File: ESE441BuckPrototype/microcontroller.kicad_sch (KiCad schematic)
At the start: 9 parts

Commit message: Add component names, values, PWM jumper
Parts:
- J?: footprint (none) -> Connector_PinHeader_2.54mm:PinHeader_2x04_P2.54mm_Vertical
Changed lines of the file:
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@@
     (property "Reference" "J?" (id 0) (at 228.6 82.55 0))
     (property "Value" "ICSP" (id 1) (at 228.6 85.09 0))
-    (property "Footprint" "" (id 2) (at 227.33 91.44 0)
+    (property "Footprint" "Connector_PinHeader_2.54mm:PinHeader_2x04_P2.54mm_Vertical" (id 2) (at 227.33 91.44 0)
       (effects (font (size 1.27 1.27)) hide)
     )

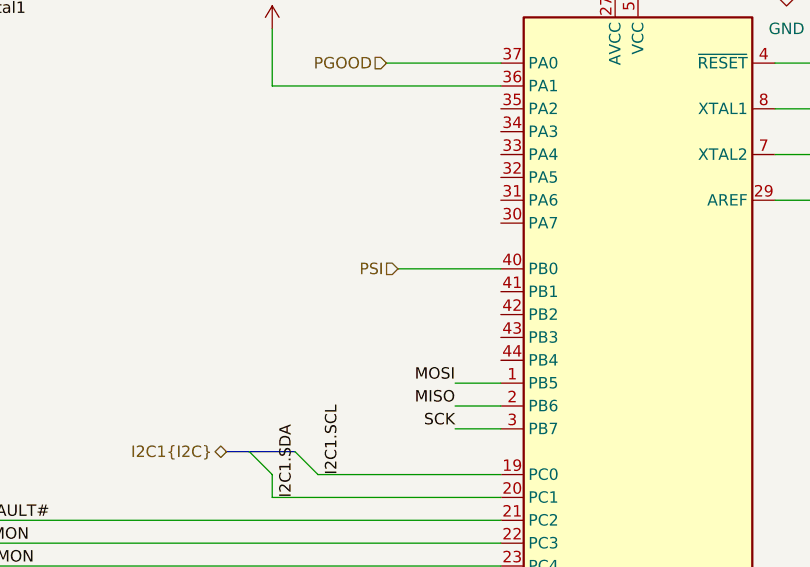
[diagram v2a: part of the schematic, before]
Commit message: Add ALERT# monitoring and fix input/output sheet pins
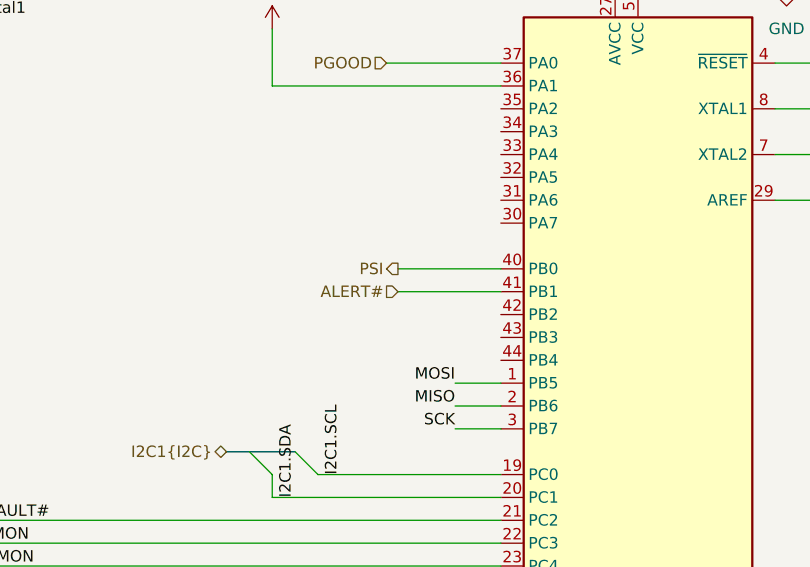
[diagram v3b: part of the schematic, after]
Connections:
- net ALERT#: now reaches U?.41 (PB1)
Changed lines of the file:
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@@
+    (stroke (width 0) (type default) (color 0 0 0 0))
+  )
+  (wire (pts (xy 123.19 95.25) (xy 134.62 95.25))
     (stroke (width 0) (type default) (color 0 0 0 0))
   )
@@
     (effects (font (size 1.27 1.27)) (justify right))
   )
+  (hierarchical_label "ALERT#" (shape input) (at 123.19 95.25 180)
+    (effects (font (size 1.27 1.27)) (justify right))
+  )
   (hierarchical_label "PMon3{PMon}" (shape input) (at 50.8 118.11 180)
     (effects (font (size 1.27 1.27)) (justify right))
   )
-  (hierarchical_label "PSI" (shape input) (at 123.19 92.71 180)
-    (effects (font (size 1.27 1.27)) (justify right))
-  )
+  (hierarchical_label "PSI" (shape output) (at 123.19 92.71 180)
+    (effects (font (size 1.27 1.27)) (justify right))
+  )

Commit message: Add optional LDO and annotations
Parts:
- added C39: 1u-DNP, symbol Device:C_Small
- added C40: 0.1u, symbol Device:C_Small
- added J2, J3: Header, symbol Connector_Generic:Conn_01x02
- added JP2, JP3: Jumper_Open, symbol Jumper:SolderJumper_2_Open
- added JP4: Jumper_Bridged, symbol Jumper:SolderJumper_2_Bridged
- added U5: HT7550-1, Package_TO_SOT_SMD:SOT-23-3, symbol CustomPartsLibrary:HT7550-1
- gave numbers to parts that had none: 9
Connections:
- net +5V: now also J3.1 (Pin_1), JP4.1 (A); no longer C41.1, C42.1, R39.1, U6.17 (VCC), U6.27 (AVCC), U6.38 (VCC), U6.5 (VCC)
- net GND: now also C39.2, C40.2, U5.1 (GND)
- new net: C39.1, JP2.1 (A), U5.2 (VIN)
- new net: C40.1, C41.1, C42.1, J2.2 (Pin_2), J3.2 (Pin_2), JP3.1 (A), JP4.2 (B), R39.1, U6.17 (VCC), U6.27 (AVCC), U6.38 (VCC), U6.5 (VCC)
- new net: J2.1 (Pin_1), JP3.2 (B), U5.3 (VOUT)
- new net VIN: JP2.2 (B)

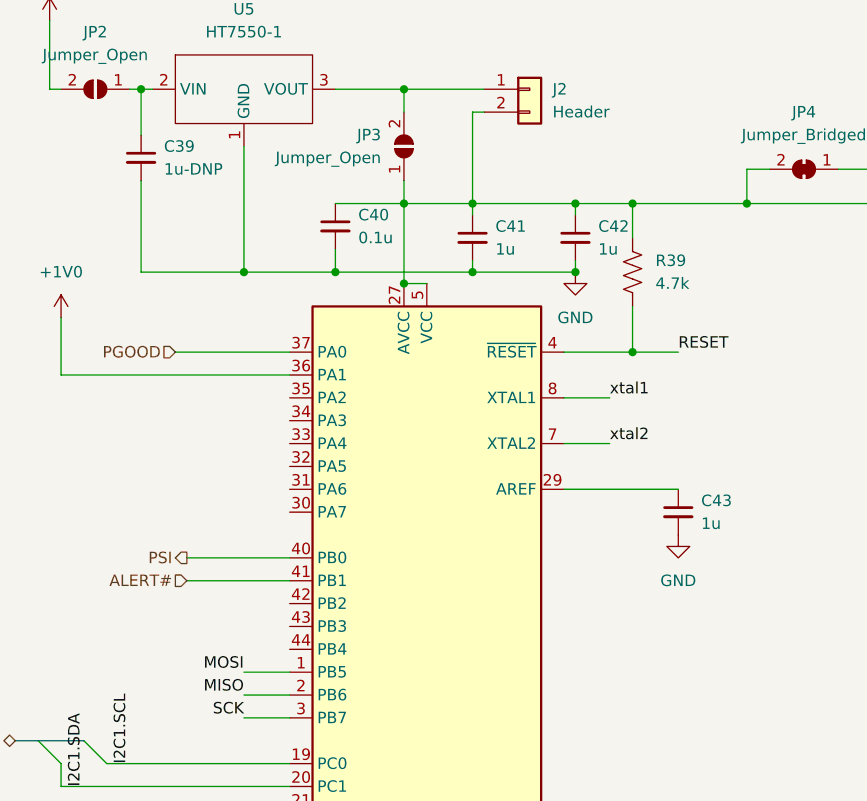
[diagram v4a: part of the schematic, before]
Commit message: Connect enable to MCU; Testpoints
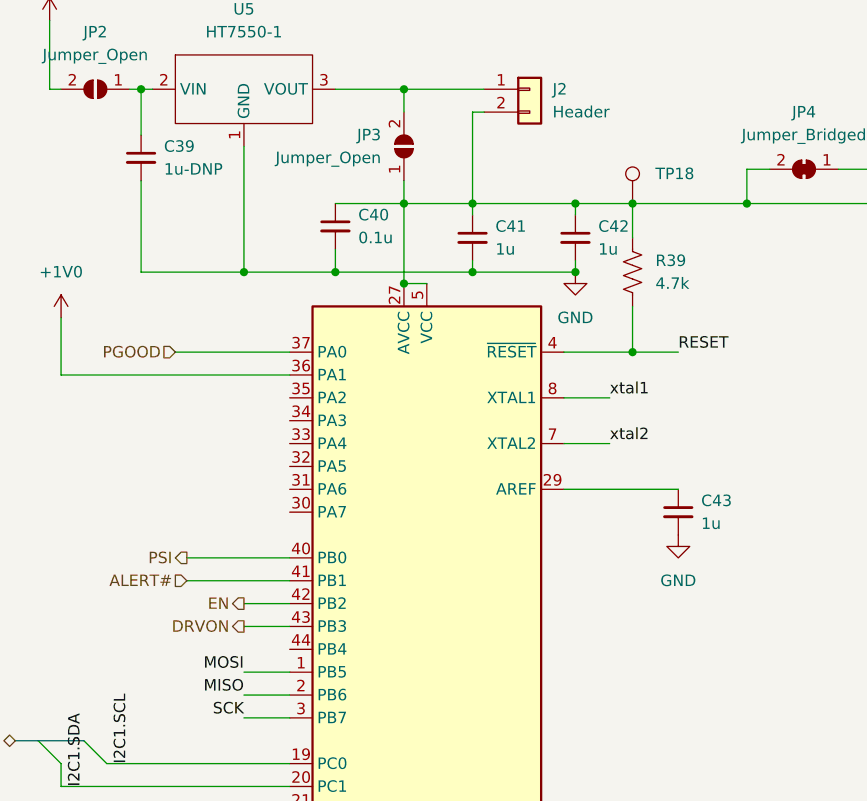
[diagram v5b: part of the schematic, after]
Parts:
- added TP18: TestPoint, TestPoint:TestPoint_Loop_D2.50mm_Drill1.0mm_LowProfile, symbol Connector:TestPoint
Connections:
- net at C40.1, C41.1, C42.1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: now also TP18.1
- net EN: now reaches U6.42 (PB2)
- net DRVON: now reaches U6.43 (PB3)
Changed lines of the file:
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@@
+    (stroke (width 0) (type default) (color 0 0 0 0))
+  )
+  (wire (pts (xy 129.54 100.33) (xy 134.62 100.33))
+    (stroke (width 0) (type default) (color 0 0 0 0))
+  )
+  (wire (pts (xy 129.54 97.79) (xy 134.62 97.79))
     (stroke (width 0) (type default) (color 0 0 0 0))
   )
@@
     (effects (font (size 1.27 1.27)) (justify right))
   )
+  (hierarchical_label "EN" (shape output) (at 129.54 97.79 180)
+    (effects (font (size 1.27 1.27)) (justify right))
+  )
   (hierarchical_label "ALERT#" (shape input) (at 123.19 95.25 180)
     (effects (font (size 1.27 1.27)) (justify right))
@@
     (effects (font (size 1.27 1.27)) (justify right))
   )
+  (hierarchical_label "DRVON" (shape output) (at 129.54 100.33 180)
+    (effects (font (size 1.27 1.27)) (justify right))
+  )
+  (symbol (lib_id "Connector:TestPoint") (at 172.72 53.34 0) (unit 1)
+    (in_bom yes) (on_board yes) (fields_autoplaced)
+    (property "Reference" "TP18" (id 0) (at 175.26 50.0379 0)
+      (effects (font (size 1.27 1.27)) (justify left))
+    )
+    (property "Value" "TestPoint" (id 1) (at 175.26 51.3079 0)
+      (effects (font (size 1.27 1.27)) (justify left) hide)
+    )
+    (property "Footprint" "TestPoint:TestPoint_Loop_D2.50mm_Drill1.0mm_LowProfile" (id 2) (at 177.8 53.34 0)
+      (effects (font (size 1.27 1.27)) hide)
+    )
+    (property "Datasheet" "~" (id 3) (at 177.8 53.34 0)
+      (effects (font (size 1.27 1.27)) hide)
+    )
+    (pin "1")
+  )
   (symbol (lib_id "Jumper:SolderJumper_2_Open") (at 113.03 40.64 180) (unit 1)
